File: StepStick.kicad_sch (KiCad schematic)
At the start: 5 parts, among them J1001 Conn_01x02_Male, J1002 Conn_01x08_Female, J1003 Screw_Terminal_01x04, J1004 Conn_02x02_Odd_Even, J1005 Conn_01x08_Female

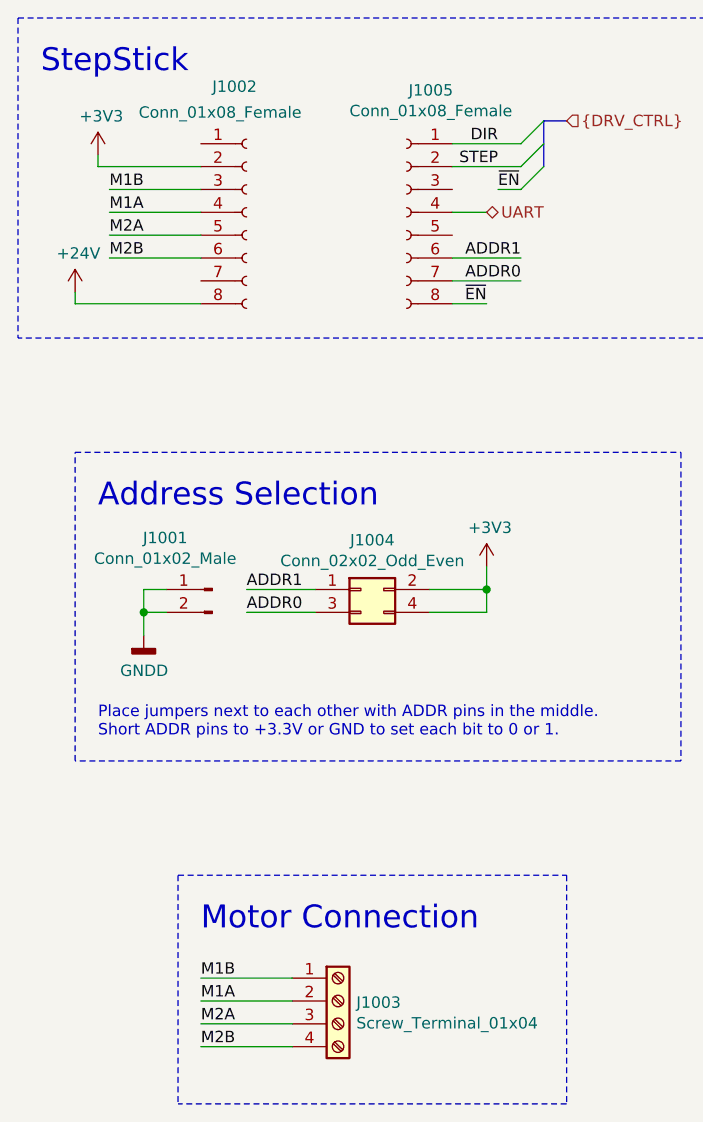
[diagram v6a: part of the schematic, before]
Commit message: Fix footprint associations, use 74LVC2G07 instead of MOSFETs
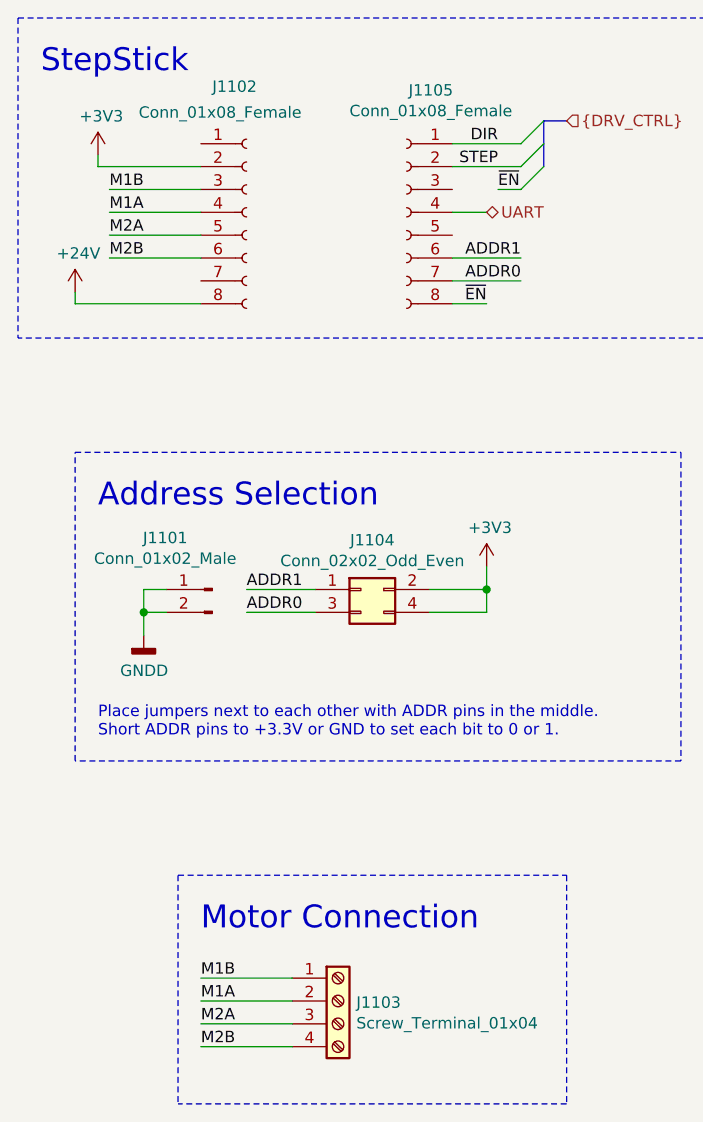
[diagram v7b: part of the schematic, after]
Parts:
- J1101: renamed from J1001; footprint (none) -> Connector_PinHeader_2.54mm:PinHeader_1x02_P2.54mm_Vertical
- J1102: renamed from J1002; footprint (none) -> Connector_PinSocket_2.54mm:PinSocket_1x08_P2.54mm_Vertical
- J1103: renamed from J1003; footprint (none) -> TerminalBlock_Phoenix:TerminalBlock_Phoenix_PT-1,5-4-5.0-H_1x04_P5.00mm_Horizontal
- J1104: renamed from J1004; footprint (none) -> Connector_PinHeader_2.54mm:PinHeader_2x02_P2.54mm_Vertical
- J1105: renamed from J1005; footprint (none) -> Connector_PinSocket_2.54mm:PinSocket_1x08_P2.54mm_Vertical
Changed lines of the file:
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@@
   (symbol (lib_id "power:+24V") (at 116.84 63.5 0)
     (in_bom yes) (on_board yes)
-    (property "Reference" "#PWR01001" (id 0) (at 116.84 67.31 0)
+    (property "Reference" "#PWR01101" (id 0) (at 116.84 67.31 0)
       (effects (font (size 1.27 1.27)) hide)
     )
@@
   (symbol (lib_id "power:+3V3") (at 119.38 48.26 0)
     (in_bom yes) (on_board yes)
-    (property "Reference" "#PWR01002" (id 0) (at 119.38 52.07 0)
+    (property "Reference" "#PWR01102" (id 0) (at 119.38 52.07 0)
       (effects (font (size 1.27 1.27)) hide)
     )
@@
   (symbol (lib_id "power:+3V3") (at 162.56 93.98 0)
     (in_bom yes) (on_board yes)
-    (property "Reference" "#PWR01004" (id 0) (at 162.56 97.79 0)
+    (property "Reference" "#PWR01104" (id 0) (at 162.56 97.79 0)
       (effects (font (size 1.27 1.27)) hide)
     )
@@
   (symbol (lib_id "power:GNDD") (at 124.46 101.6 0)
     (in_bom yes) (on_board yes)
-    (property "Reference" "#PWR01003" (id 0) (at 124.46 107.95 0)
+    (property "Reference" "#PWR01103" (id 0) (at 124.46 107.95 0)
       (effects (font (size 1.27 1.27)) hide)
     )
@@
   (symbol (lib_id "Connector:Conn_01x02_Male") (at 132.08 96.52 0) (mirror y)
     (in_bom yes) (on_board yes)
-    (property "Reference" "J1001" (id 0) (at 126.8476 90.7858 0))
+    (property "Reference" "J1101" (id 0) (at 126.8476 90.7858 0))
     (property "Value" "Conn_01x02_Male" (id 1) (at 126.8476 93.0845 0))
-    (property "Footprint" "" (id 2) (at 132.08 96.52 0)
+    (property "Footprint" "Connector_PinHeader_2.54mm:PinHeader_1x02_P2.54mm_Vertical" (id 2) (at 132.08 96.52 0)
       (effects (font (size 1.27 1.27)) hide)
     )
@@
   (symbol (lib_id "Connector:Screw_Terminal_01x04") (at 146.05 142.24 0)
     (in_bom yes) (on_board yes)
-    (property "Reference" "J1003" (id 0) (at 148.0821 142.4114 0)
+    (property "Reference" "J1103" (id 0) (at 148.0821 142.4114 0)
       (effects (font (size 1.27 1.27)) (justify left))
     )
@@
       (effects (font (size 1.27 1.27)) (justify left))
     )
-    (property "Footprint" "" (id 2) (at 146.05 142.24 0)
+    (property "Footprint" "TerminalBlock_Phoenix:TerminalBlock_Phoenix_PT-1,5-4-5.0-H_1x04_P5.00mm_Horizontal" (id 2) (at 146.05 142.24 0)
       (effects (font (size 1.27 1.27)) hide)
     )
@@
   (symbol (lib_id "Connector_Generic:Conn_02x02_Odd_Even") (at 148.59 96.52 0)
     (in_bom yes) (on_board yes)
-    (property "Reference" "J1004" (id 0) (at 149.86 91.0398 0))
+    (property "Reference" "J1104" (id 0) (at 149.86 91.0398 0))
     (property "Value" "Conn_02x02_Odd_Even" (id 1) (at 149.86 93.3385 0))
-    (property "Footprint" "" (id 2) (at 148.59 96.52 0)
+    (property "Footprint" "Connector_PinHeader_2.54mm:PinHeader_2x02_P2.54mm_Vertical" (id 2) (at 148.59 96.52 0)
       (effects (font (size 1.27 1.27)) hide)
     )
@@
   (symbol (lib_id "Connector:Conn_01x08_Female") (at 135.89 54.61 0)
     (in_bom yes) (on_board yes)
-    (property "Reference" "J1002" (id 0) (at 132.08 40.64 0)
+    (property "Reference" "J1102" (id 0) (at 132.08 40.64 0)
       (effects (font (size 1.27 1.27)) (justify left))
     )
@@
       (effects (font (size 1.27 1.27)) (justify left))
     )
-    (property "Footprint" "" (id 2) (at 135.89 54.61 0)
+    (property "Footprint" "Connector_PinSocket_2.54mm:PinSocket_1x08_P2.54mm_Vertical" (id 2) (at 135.89 54.61 0)
       (effects (font (size 1.27 1.27)) hide)
     )
@@
   (symbol (lib_id "Connector:Conn_01x08_Female") (at 153.67 54.61 0) (mirror y)
     (in_bom yes) (on_board yes)
-    (property "Reference" "J1005" (id 0) (at 156.3624 41.0526 0))
+    (property "Reference" "J1105" (id 0) (at 156.3624 41.0526 0))
     (property "Value" "Conn_01x08_Female" (id 1) (at 156.3624 43.3513 0))
-    (property "Footprint" "" (id 2) (at 153.67 54.61 0)
+    (property "Footprint" "Connector_PinSocket_2.54mm:PinSocket_1x08_P2.54mm_Vertical" (id 2) (at 153.67 54.61 0)
       (effects (font (size 1.27 1.27)) hide)
     )

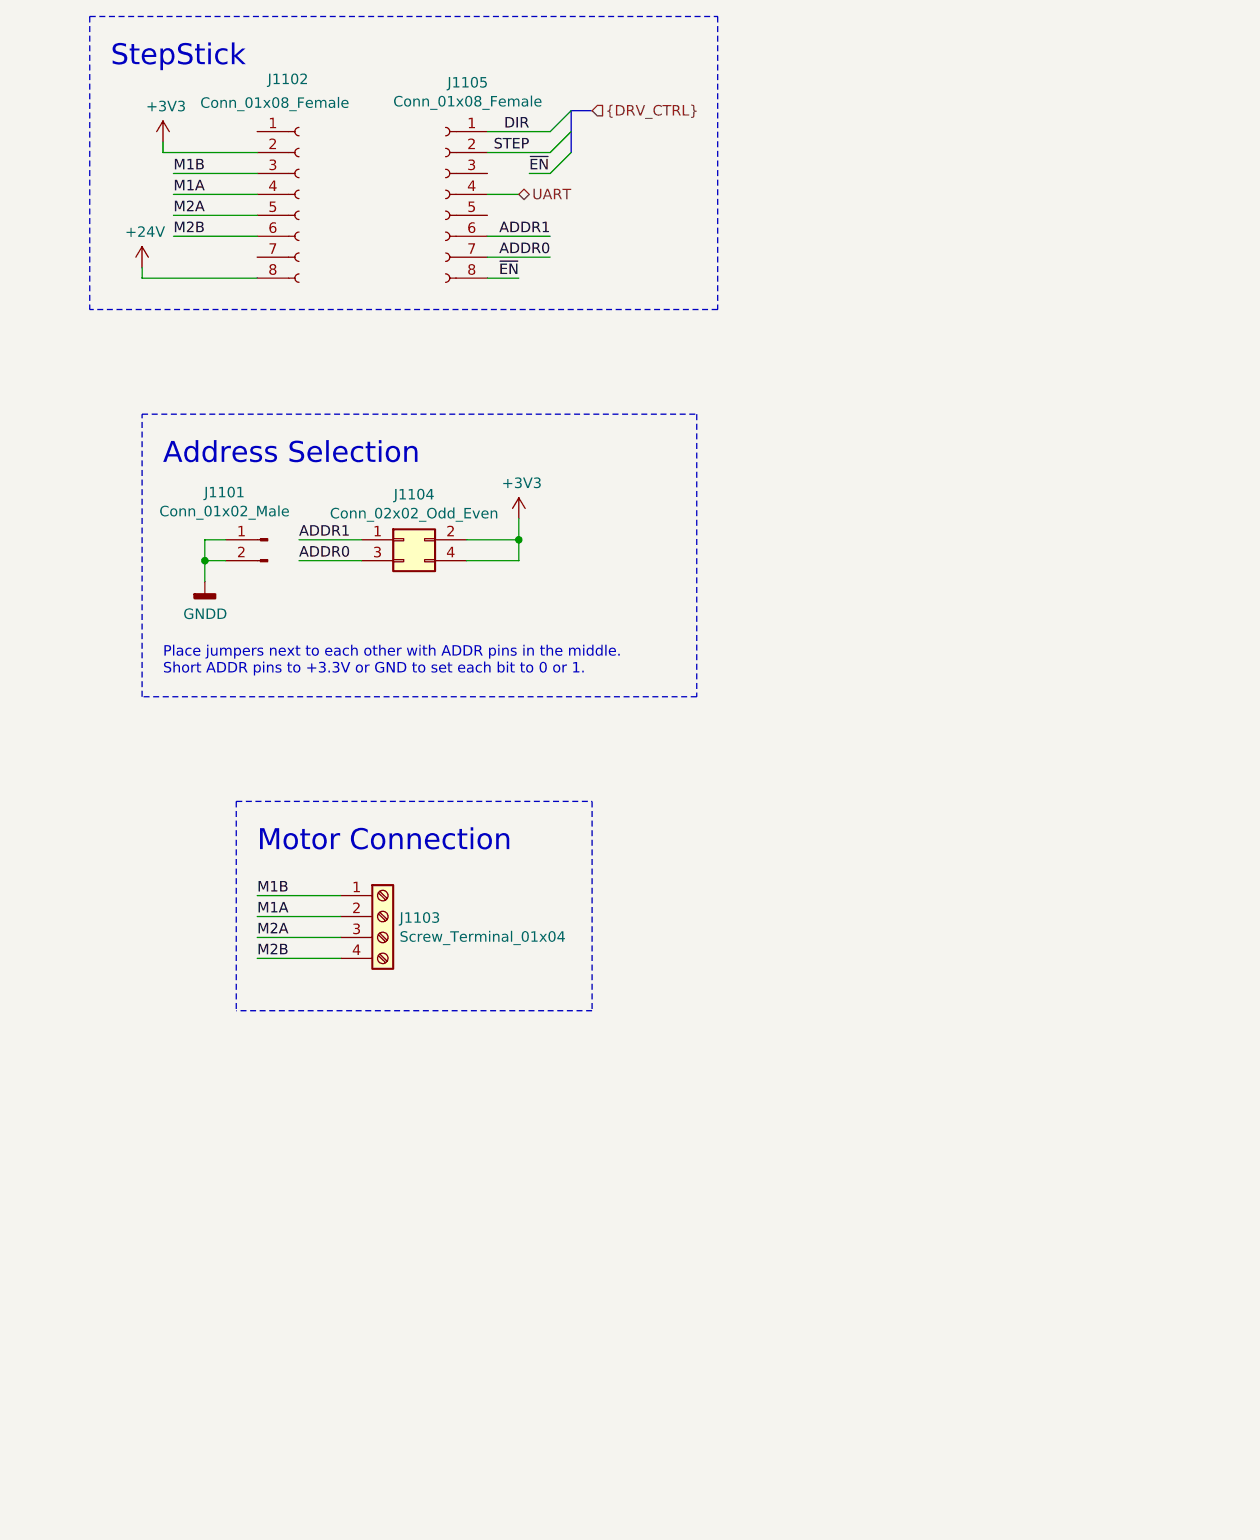
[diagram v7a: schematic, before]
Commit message: Connect Ethernet and USB to MIO, start layout
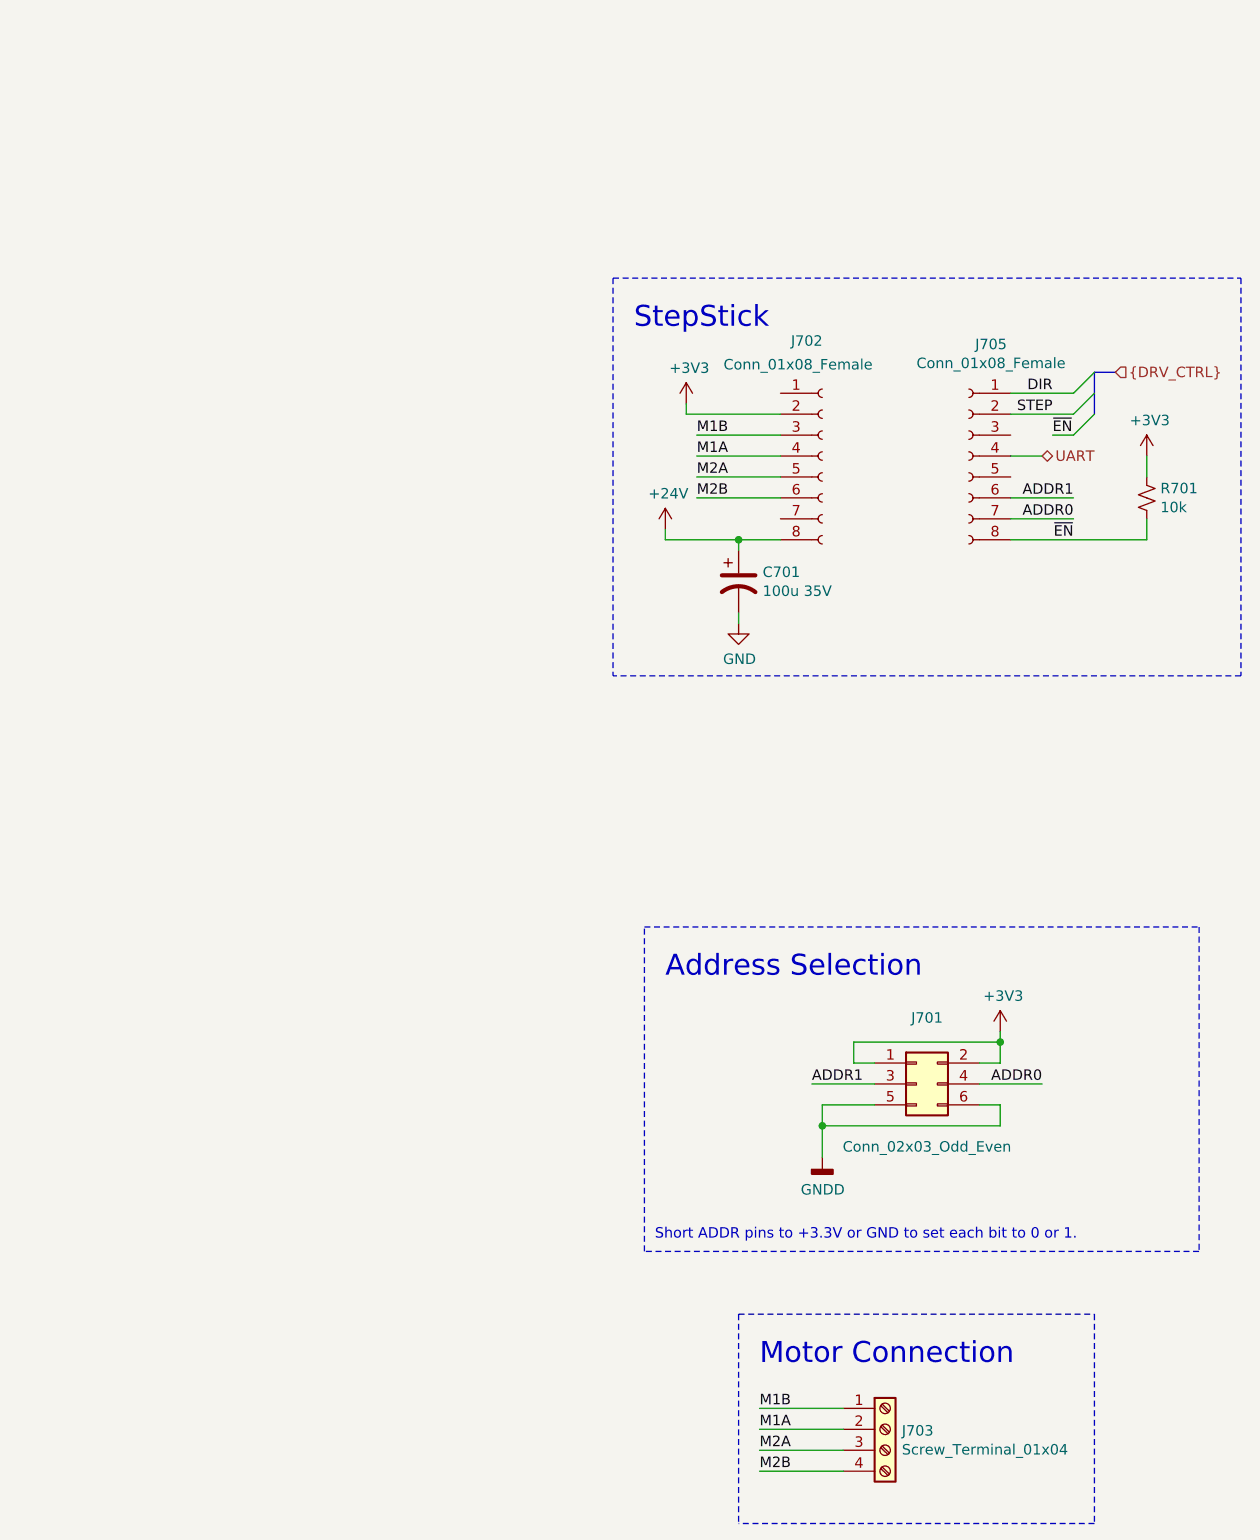
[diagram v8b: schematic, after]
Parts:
- removed J1101: Conn_01x02_Male, Connector_PinHeader_2.54mm:PinHeader_1x02_P2.54mm_Vertical, symbol Connector:Conn_01x02_Male
- removed J1104: Conn_02x02_Odd_Even, Connector_PinHeader_2.54mm:PinHeader_2x02_P2.54mm_Vertical, symbol Connector_Generic:Conn_02x02_Odd_Even
- added C701: 100u 35V, Capacitor_SMD:CP_Elec_5x3, symbol Device:CP1
- added J701: Conn_02x03_Odd_Even, Connector_PinHeader_2.54mm:PinHeader_2x03_P2.54mm_Vertical, symbol Connector_Generic:Conn_02x03_Odd_Even
- added R701: 10k, Resistor_SMD:R_0603_1608Metric, symbol Device:R_Small_US
- renumbered J1102 to J702, J1103 to J703, J1105 to J705
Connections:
- net +24V: now also C701.1
- net +3V3: now also J701.1 (Pin_1), J701.2 (Pin_2), R701.1
- net ADDR0: now also J701.4 (Pin_4)
- net ADDR1: now also J701.3 (Pin_3)
- net GNDD: now also J701.5 (Pin_5), J701.6 (Pin_6)
- net ~EN: now also R701.2
- new net GND: C701.2
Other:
- note added: "Short ADDR pins to +3.3V or GND to set each bit to 0 or 1."
- note removed: "Place jumpers next to each other with ADDR pins in the middle. Short ADDR pins to +3.3V or GND to set each bit to 0 or 1."
- moved on the sheet: J702, J703, J705
